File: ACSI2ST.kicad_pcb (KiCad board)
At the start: 2 copper layers, 52.9 x 64.7 mm, 56 parts, among them J10 RESET, J11 FLASH, J12 ID_SHIFT, J13 STRICT, J14 UART, P1 IDC20, U1 XC6206PxxxMR, U2 STM32F103C8Tx, X1 32.768KHz, X2 8MHz

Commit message: use single pins for db19
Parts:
- removed H1, H2: MountingHole, MountingHole:MountingHole_3.2mm_M3
- removed J1, J2, J3, J4, J5, J6, J7, J8, J9: ~, Connector_PinHeader_2.54mm:PinHeader_1x02_P2.54mm_Vertical
- added P2: DB-19 Male, ACSI2ST:DSUB-19_Pins_Vertical, F.Cu at (156.6, 111.6)
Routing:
- net /PA9: track 42.0 -> 40.7 mm
- net GND: vias 28 -> 33
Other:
- board text added: "1"
- board text added: "11"

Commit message: refine pcb layout
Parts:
- moved J11 3.33 mm to (139.8, 98.8)
- moved J12 3.23 mm to (136.1, 98.8)
- moved J14 3.23 mm to (132.5, 98.0)
- moved C1 3.03 mm to (133.2, 89.1)
- moved J13 3.00 mm to (143.1, 98.8)
- moved J10 2.97 mm to (142.3, 106.6)
- moved BT1 2.95 mm to (156.5, 91.2)
- moved C2 2.76 mm to (143.3, 87.3)
- moved C17 2.63 mm to (139.4, 86.2)
- moved R11 2.56 mm to (140.3, 92.2)
- moved R10 2.54 mm to (140.3, 90.6)
- moved U1 2.41 mm to (136.6, 89.6)
- moved R5 2.24 mm to (151.2, 100.1)
- moved R6 2.24 mm to (151.2, 103.4)
- moved C6 2.08 mm to (149.1, 103.3)
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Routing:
- net VDD: track 179.9 -> 171.4 mm
- net /PA14: track 48.3 -> 44.1 mm
- net /PA13: track 37.2 -> 33.3 mm
- net /PA9: track 40.7 -> 37.4 mm
- net /BOOT0: track 40.0 -> 36.9 mm
- net Net-(USB1-CC1): track 4.97 -> 7.75 mm
- net /VBatt: track 34.8 -> 32.5 mm
- net /PA10: track 42.3 -> 40.0 mm
- net /PB2: track 32.5 -> 30.4 mm
- net /RESET: track 38.7 -> 36.9 mm
- net Net-(J14-Pin_1): track 18.5 -> 16.8 mm
- net /PC13: track 71.8 -> 73.1 mm
- net /PA5: track 56.4 -> 55.5 mm
- net /PA8: track 25.3 -> 26.2 mm
- net Net-(USB1-CC2): track 5.09 -> 5.78 mm
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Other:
- board size 52.9 x 64.7 mm -> 51 x 64.7 mm

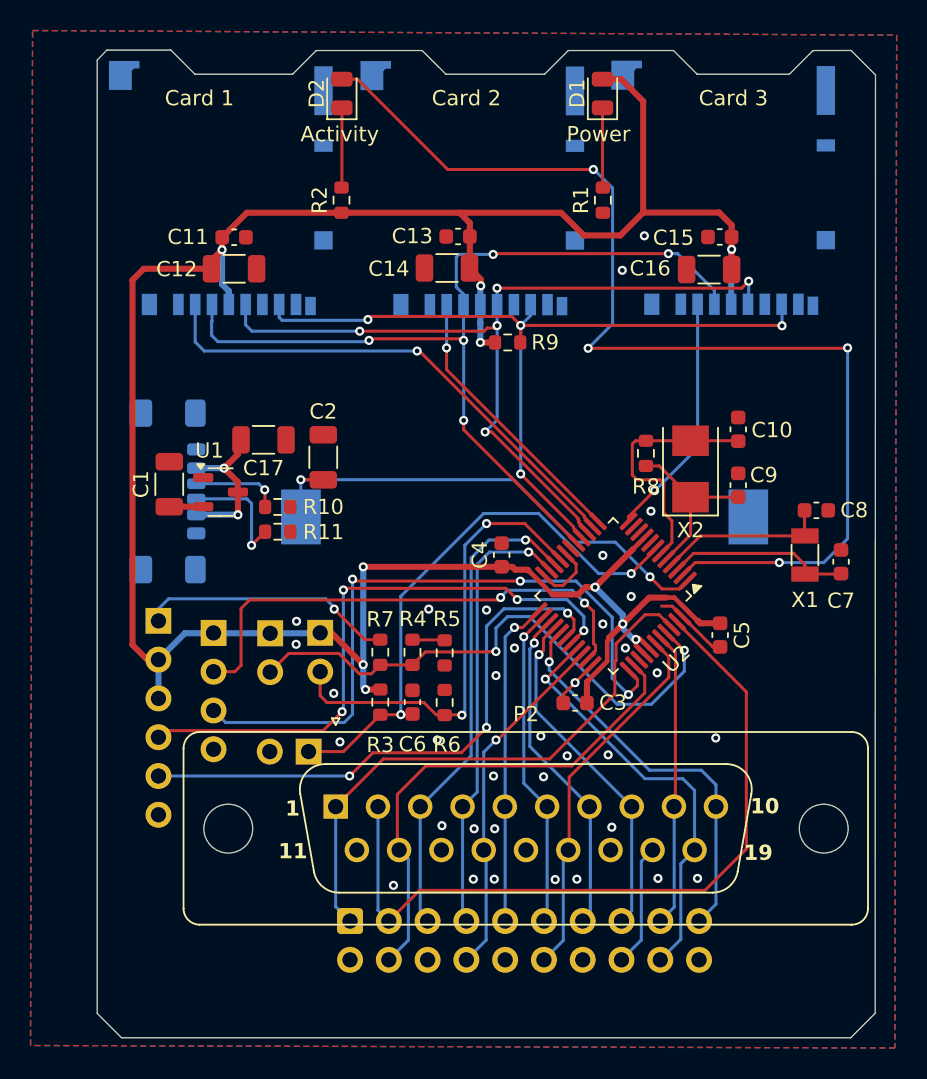
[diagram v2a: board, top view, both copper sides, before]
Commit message: fix drc violations
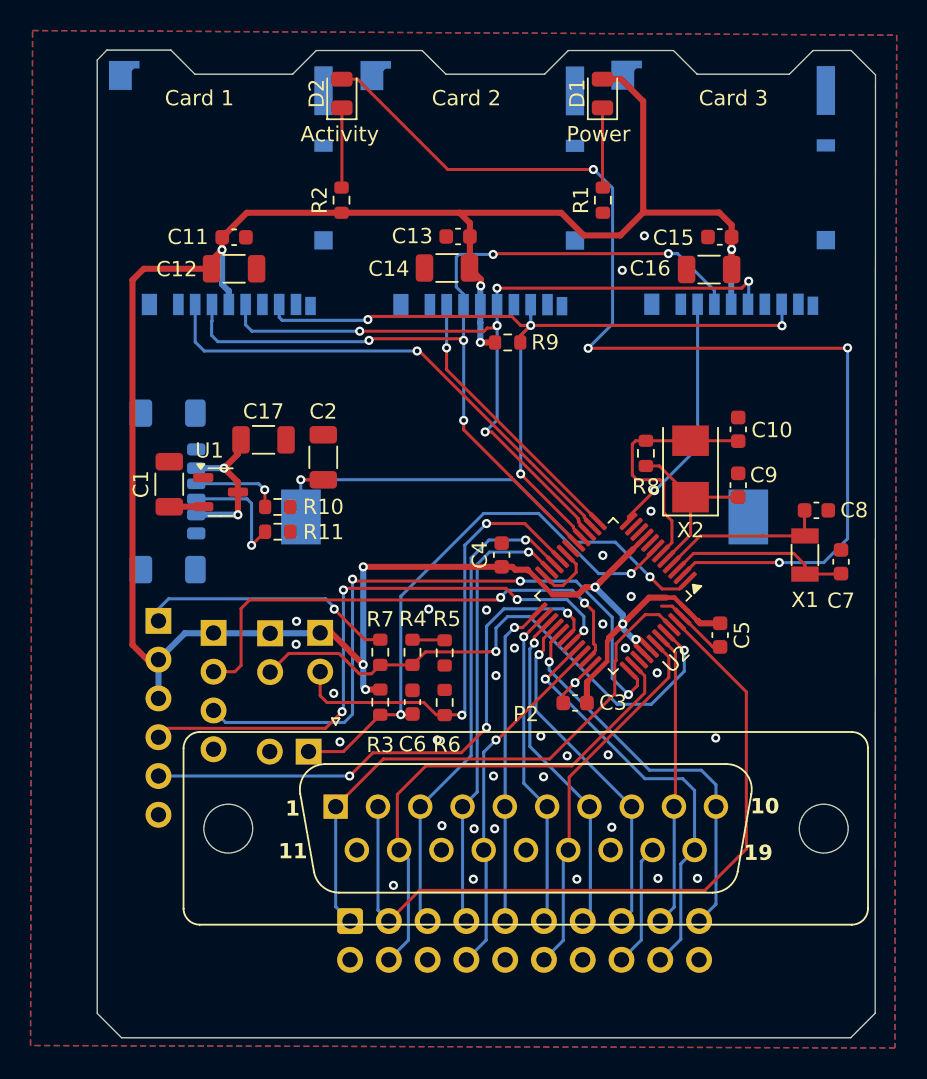
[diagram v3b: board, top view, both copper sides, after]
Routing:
- net GND: vias 35 -> 33
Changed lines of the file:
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@@
 		(tags "capacitor")
 		(property "Reference" "C17"
-			(at 0 1.8542 0)
+			(at 0 -1.8574 0)
 			(layer "F.SilkS")
 			(effects
@@
 	)
 	(via
-		(at 154.4828 114.935)
-		(size 0.6)
-		(drill 0.3)
-		(layers "F.Cu" "B.Cu")
-		(free yes)
-		(net 2)
-	)
-	(via
 		(at 164.7444 90.8304)
 		(size 0.6)
@@
 	)
 	(via
-		(at 158.4706 114.9604)
-		(size 0.6)
-		(drill 0.3)
-		(layers "F.Cu" "B.Cu")
-		(free yes)
-		(net 2)
-	)
-	(via
 		(at 161.94007 106.79193)
 		(size 0.6)
@@
 	)
 	(segment
-		(start 156.21 78.6638)
-		(end 173.3042 78.6638)
+		(start 156.21 79.3242)
+		(end 156.21 79.756)
 		(width 0.2)
 		(layer "F.Cu")
@@
 	)
 	(segment
-		(start 155.6258 78.0796)
-		(end 156.21 78.6638)
+		(start 156.8704 78.6638)
+		(end 156.21 79.3242)
 		(width 0.2)
 		(layer "F.Cu")
@@
 	)
 	(segment
-		(start 156.21 79.756)
-		(end 156.1846 79.7814)
+		(start 156.8704 78.6638)
+		(end 173.3042 78.6638)
 		(width 0.2)
 		(layer "F.Cu")
@@
 	)
 	(segment
-		(start 146.2024 78.2828)
-		(end 146.4056 78.0796)
+		(start 156.8704 78.6638)
+		(end 156.21 78.6638)
 		(width 0.2)
 		(layer "F.Cu")
@@
 	)
 	(segment
-		(start 156.21 78.6638)
-		(end 156.21 79.756)
+		(start 156.21 79.756)
+		(end 156.1846 79.7814)
 		(width 0.2)
 		(layer "F.Cu")
@@
 	)
 	(segment
-		(start 173.3042 78.6638)
-		(end 173.3296 78.6892)
+		(start 156.21 78.6638)
+		(end 155.6258 78.0796)
 		(width 0.2)
 		(layer "F.Cu")
@@
 	)
 	(segment
-		(start 146.4056 78.0796)
-		(end 155.6258 78.0796)
+		(start 159.669602 91.853132)
+		(end 156.209235 88.392765)
 		(width 0.2)
 		(layer "F.Cu")
@@
 	)
 	(segment
-		(start 159.669602 91.853132)
-		(end 156.209235 88.392765)
+		(start 155.6258 78.0796)
+		(end 146.4056 78.0796)
 		(width 0.2)
 		(layer "F.Cu")
@@
 		(net 13)
 	)
+	(segment
+		(start 173.3042 78.6638)
+		(end 173.3296 78.6892)
+		(width 0.2)
+		(layer "F.Cu")
+		(net 13)
+	)
+	(segment
+		(start 146.4056 78.0796)
+		(end 146.2024 78.2828)
+		(width 0.2)
+		(layer "F.Cu")
+		(net 13)
+	)
 	(via
 		(at 146.2024 78.2828)
@@
 	)
 	(via
-		(at 156.21 78.6638)
+		(at 156.8704 78.6638)
 		(size 0.6)
 		(drill 0.3)
@@
 	)
 	(segment
+		(start 156.8704 78.6638)
+		(end 156.21 79.3242)
+		(width 0.2)
+		(layer "B.Cu")
+		(net 13)
+	)
+	(segment
+		(start 156.21 79.3242)
+		(end 156.21 88.392)
+		(width 0.2)
+		(layer "B.Cu")
+		(net 13)
+	)
+	(segment
 		(start 146.1516 78.3336)
 		(end 140.589 78.3336)
@@
 	)
 	(segment
-		(start 156.21 78.6638)
-		(end 156.21 88.392)
+		(start 156.8704 78.6638)
+		(end 156.8704 78.0122)
 		(width 0.2)
 		(layer "B.Cu")
@@
 	)
 	(segment
-		(start 173.3296 77.308)
-		(end 173.2998 77.2782)
+		(start 156.866 78.0078)
+		(end 156.866 77.3036)
 		(width 0.2)
 		(layer "B.Cu")
@@
 	)
 	(segment
-		(start 146.2024 78.2828)
-		(end 146.1516 78.3336)
+		(start 173.3296 77.308)
+		(end 173.2998 77.2782)
 		(width 0.2)
 		(layer "B.Cu")
@@
 	)
 	(segment
-		(start 156.866 77.3036)
-		(end 156.866 78.0078)
+		(start 146.2024 78.2828)
+		(end 146.1516 78.3336)
 		(width 0.2)
 		(layer "B.Cu")
@@
 	)
 	(segment
-		(start 156.866 78.0078)
-		(end 156.21 78.6638)
+		(start 156.8704 78.0122)
+		(end 156.866 78.0078)
 		(width 0.2)
 		(layer "B.Cu")
@@
 	)
 	(segment
-		(start 143.271073 105.2068)
-		(end 132.9182 105.2068)
+		(start 155.2448 95.885)
+		(end 155.9814 96.6216)
 		(width 0.2)
 		(layer "F.Cu")
@@
 	)
 	(segment
-		(start 155.2448 95.885)
-		(end 155.9814 96.6216)
+		(start 144.513673 103.9642)
+		(end 143.423473 105.0544)
 		(width 0.2)
 		(layer "F.Cu")
@@
 	)
 	(segment
-		(start 144.513673 103.9642)
-		(end 143.271073 105.2068)
+		(start 143.423473 105.0544)
+		(end 133.0706 105.0544)
+		(width 0.2)
+		(layer "F.Cu")
+		(net 52)
+	)
+	(segment
+		(start 133.0706 105.0544)
+		(end 132.9182 105.2068)
 		(width 0.2)
 		(layer "F.Cu")

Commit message: more refinement
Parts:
- moved R9 5.08 mm to (157.2, 75.1)
- moved BT1 2.11 mm to (158.6, 91.2)
- moved J10 1.93 mm to (142.4, 104.6)
- moved R11 1.93 mm to (142.2, 92.4)
- moved R10 1.92 mm to (142.2, 90.6)
- moved USB1 1.34 mm to (133.3, 89.5)
- moved C11 1.21 mm to (138.7, 72.9)
- moved C12 1.21 mm to (138.7, 74.9)
- moved C13 1.21 mm to (153.3, 72.8)
- moved C14 1.21 mm to (152.6, 74.9)
- moved C15 1.21 mm to (170.5, 72.9)
- moved C16 1.21 mm to (169.8, 75.0)
- moved CARD1 1.21 mm to (137.8, 69.7)
- moved CARD2 1.21 mm to (154.3, 69.7)
- moved CARD3 1.21 mm to (170.7, 69.6)
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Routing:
- net /PC13: track 73.1 -> 69.6 mm
- net /VBatt: track 32.5 -> 29.9 mm
- net /PA14: track 44.1 -> 46.2 mm
- net VDD: track 171.4 -> 173.3 mm, vias 10 -> 9
- net /PA5: track 55.5 -> 53.7 mm
- net /PA10: track 40.0 -> 41.7 mm
- net /PA4: track 33.6 -> 32.4 mm
- net /RESET: track 36.9 -> 36.0 mm
- net /PA7: track 59.7 -> 58.9 mm
- net Net-(USB1-CC2): track 5.78 -> 6.36 mm
- net /PA6: track 54.2 -> 54.8 mm, vias 4 -> 5
- net /PA2: track 16.1 -> 16.6 mm
- net GND: vias 33 -> 35
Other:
- board size 51 x 64.7 mm -> 49.6 x 64.7 mm
- board text added: "J10 - RESET J11 - FLASH J12 - ID SHIFT J13 - STRICT J14 - UART"

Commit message: Final update in preparation for fabrication
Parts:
- added H1: MountingHole, MountingHole:MountingHole_2.5mm, F.Cu at (174.5, 82.4)
- added H2: MountingHole, MountingHole:MountingHole_2.5mm, F.Cu at (142.4, 83.5)
- added J1: 5V PWR, Connector_PinHeader_2.54mm:PinHeader_1x02_P2.54mm_Vertical, F.Cu at (138.8, 92.0)
- J14: moved to F.Cu
- moved C17 5.26 mm to (136.4, 82.0), turned to 180 degrees
- moved C2 4.88 mm to (148.1, 86.3), turned to 0 degrees
- moved U1 3.62 mm to (137.7, 86.0)
- moved USB1 3.61 mm to (133.3, 85.9)
- moved C1 3.43 mm to (134.0, 85.6)
- moved J14 3.20 mm to (132.6, 94.8), turned to 90 degrees
- moved R11 2.47 mm to (142.2, 89.9)
- moved R10 2.47 mm to (142.2, 88.1)
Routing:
- net /PA10: track 41.7 -> 23.7 mm, vias 4 -> 3
- net /PA9: track 37.4 -> 24.6 mm, vias 3 -> 4
- net VDD: track 173.3 -> 164.4 mm
- net VCC: track 9.63 -> 12.4 mm
- net /VBatt: track 29.9 -> 32.6 mm
- net /PA14: track 46.2 -> 45.0 mm
- net /PA4: track 32.4 -> 31.5 mm
- net Net-(USB1-CC1): track 8.17 -> 7.61 mm
- net /PA7: track 58.9 -> 58.4 mm
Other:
- board size 49.6 x 64.7 mm -> 49.5 x 64.7 mm
- board text added: "+5"

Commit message: tidy up
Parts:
- U2: value STM32F103C8Tx -> STM32F103C8T6

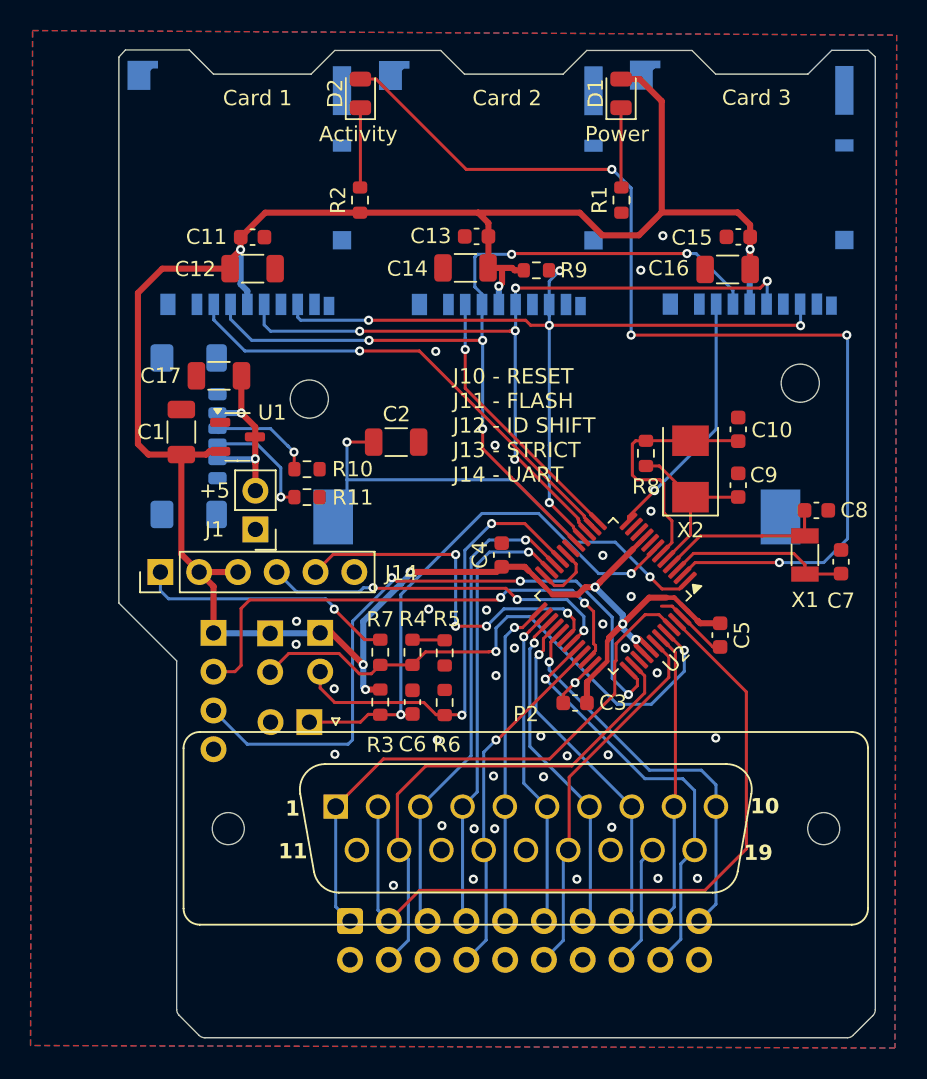
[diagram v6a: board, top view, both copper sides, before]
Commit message: add BF logo
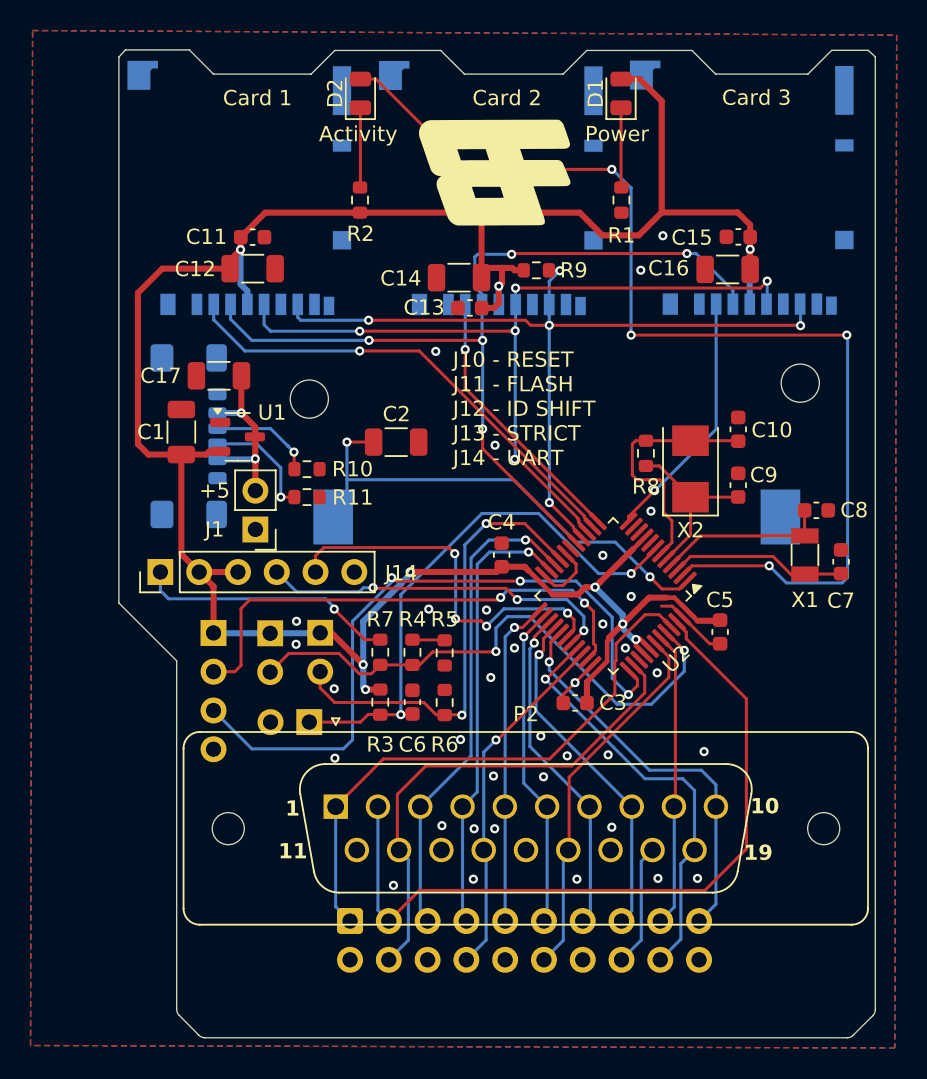
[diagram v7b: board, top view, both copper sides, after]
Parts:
- added Ge: LOGO, PowerBoard:BoardFolk, F.Cu at (154.9, 74.7)
- moved C13 4.71 mm to (152.9, 77.5)
- moved C14 0.77 mm to (152.2, 75.5)
- moved C5 0.21 mm to (169.3, 98.7)
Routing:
- net VDD: track 164.4 -> 168.0 mm
- net /PC13: track 69.6 -> 72.0 mm
- net /OSC32_in: track 12.1 -> 11.6 mm
